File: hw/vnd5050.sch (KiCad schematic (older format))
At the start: 8 parts, among them U601 VND5050AJTR-E

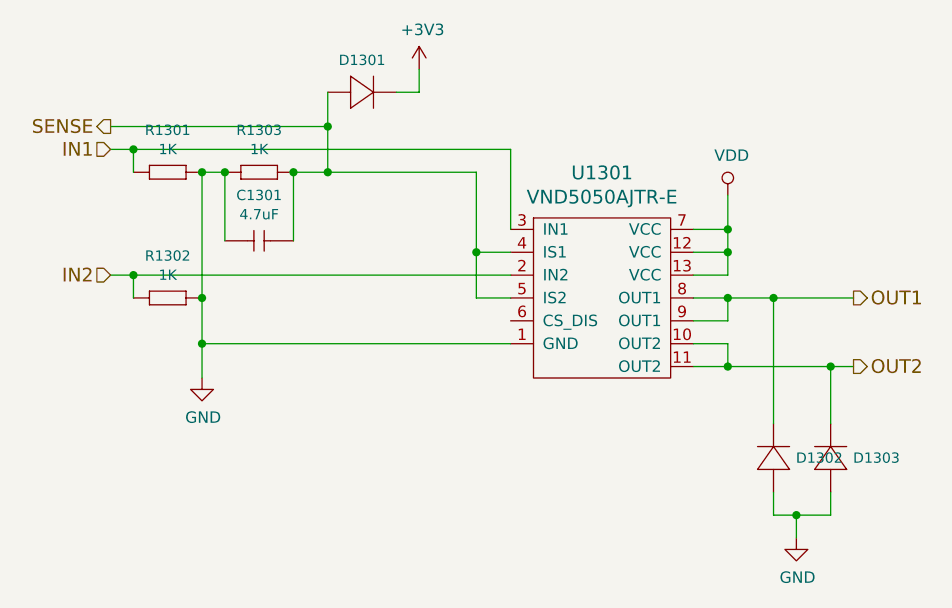
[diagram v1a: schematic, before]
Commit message: pull down resistor to boom vdd added, flyback diodes replaced with zeners
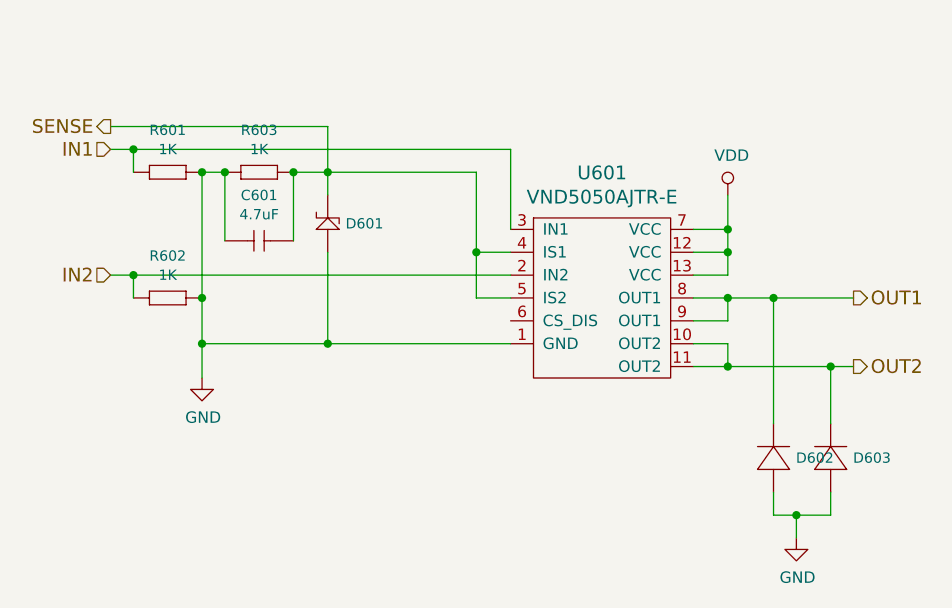
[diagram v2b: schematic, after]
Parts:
- removed D601: DIODE_RS07J-GS18, usevolt:DO219AB, symbol usevolt:DIODE_RS07J-GS18
- added D801: ZENER_MM3Z3V6T1G, usevolt:SOD-323, symbol usevolt:ZENER_MM3Z3V6T1G
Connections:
- net GND: now also D801.2
- net SENSE: now also D801.1
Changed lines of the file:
@@
 $Descr A4 11693 8268
 encoding utf-8
-Sheet 13 13
+Sheet 8 13
 Title ""
 Date ""
@@
 	2550 4000 2650 4000
 Wire Wire Line
-	2950 4300 4300 4300
+	2950 4300 3500 4300
 Wire Wire Line
 	3050 3550 2950 3550
@@
 	3350 3550 3500 3550
 Wire Wire Line
-	3500 3200 3500 3350
-Wire Wire Line
 	3500 3350 2550 3350
 Connection ~ 3500 3550
@@
 	4150 4100 4300 4100
 Connection ~ 4150 3900
-Connection ~ 3500 3350
-Wire Wire Line
-	3900 3100 3900 3200
-Wire Wire Line
-	3900 3200 3800 3200
 Wire Wire Line
 	5250 3800 5250 3900
@@
 AR Path="/5B0F1C64/5AF37914" Ref="U1201"  Part="1"
 AR Path="/5B10443F/5AF37914" Ref="U1301"  Part="1"
-F 0 "U1301" H 4700 4447 60  0000 C CNN
+F 0 "U601" H 4700 4447 60  0000 C CNN
 F 1 "VND5050AJTR-E" H 4700 4341 60  0000 C CNN
 F 2 "usevolt:PowerSSO-12" H 4600 4400 60  0001 C CNN
@@
 F 7 "VND5050AJTR-E" H 4800 4600 60  0001 C CNN "Manufacturer Part Number"
 	1    4600 4000
-	1    0    0    -1
-$EndComp
-$Comp
-L power:+3V3 #PWR0127
-U 1 1 5AF379DD
-P 3900 3100
-AR Path="/5AF2EB89/5AF379DD" Ref="#PWR0127"  Part="1"
-AR Path="/5AF65DC6/5AF379DD" Ref="#PWR0111"  Part="1"
-AR Path="/5AF66334/5AF379DD" Ref="#PWR0115"  Part="1"
-AR Path="/5AF66EB3/5AF379DD" Ref="#PWR0119"  Part="1"
-AR Path="/5AF67112/5AF379DD" Ref="#PWR0123"  Part="1"
-AR Path="/5B0F1C64/5AF379DD" Ref="#PWR01202"  Part="1"
-AR Path="/5B10443F/5AF379DD" Ref="#PWR01302"  Part="1"
-F 0 "#PWR01302" H 3900 2950 50  0001 C CNN
-F 1 "+3V3" H 3915 3273 50  0000 C CNN
-F 2 "" H 3900 3100 50  0000 C CNN
-F 3 "" H 3900 3100 50  0000 C CNN
-	1    3900 3100
-	1    0    0    -1
-$EndComp
-$Comp
-L usevolt:DIODE_RS07J-GS18 D601
-U 1 1 5AF37BFE
-P 3700 3200
-AR Path="/5AF2EB89/5AF37BFE" Ref="D601"  Part="1"
-AR Path="/5AF65DC6/5AF37BFE" Ref="D701"  Part="1"
-AR Path="/5AF66334/5AF37BFE" Ref="D801"  Part="1"
-AR Path="/5AF66EB3/5AF37BFE" Ref="D901"  Part="1"
-AR Path="/5AF67112/5AF37BFE" Ref="D1001"  Part="1"
-AR Path="/5B0F1C64/5AF37BFE" Ref="D1201"  Part="1"
-AR Path="/5B10443F/5AF37BFE" Ref="D1301"  Part="1"
-F 0 "D1301" H 3650 3340 45  0000 C CNN
-F 1 "DIODE_RS07J-GS18" H 3720 3140 45  0001 L BNN
-F 2 "usevolt:DO219AB" H 3730 3350 20  0001 C CNN
-F 3 "http://www.vishay.com/docs/85742/rs07b.pdf" H 3720 3220 60  0001 C CNN
-F 4 "1864882" H 4320 3820 60  0001 C CNN "2nd Source Part Number"
-F 5 "Digi-Key" H 4020 3520 60  0001 C CNN "1st Source"
-F 6 "Farnell" H 4220 3720 60  0001 C CNN "2nd Source"
-F 7 "RS07J-GS18" H 3920 3420 60  0001 C CNN "Manufacturer Part Number"
-F 8 "RS07J-GS18-ND" H 4120 3620 60  0001 C CNN "1st Source Part Number"
-F 9 "Vishay Semiconductor Diodes Division" H 3820 3320 60  0001 C CNN "Manufacturer"
-	1    3700 3200
 	1    0    0    -1
 $EndComp
@@
 AR Path="/5B0F1C64/5AF37D16" Ref="R1201"  Part="1"
 AR Path="/5B10443F/5AF37D16" Ref="R1301"  Part="1"
-F 0 "R1301" H 2800 3734 45  0000 C CNN
+F 0 "R601" H 2800 3734 45  0000 C CNN
 F 1 "1K" H 2800 3650 45  0000 C CNN
 F 2 "yageo:0603" H 2780 3700 20  0001 C CNN
@@
 AR Path="/5B0F1C64/5AF37DEE" Ref="R1203"  Part="1"
 AR Path="/5B10443F/5AF37DEE" Ref="R1303"  Part="1"
-F 0 "R1303" H 3200 3734 45  0000 C CNN
+F 0 "R603" H 3200 3734 45  0000 C CNN
 F 1 "1K" H 3200 3650 45  0000 C CNN
 F 2 "yageo:0603" H 3180 3700 20  0001 C CNN
@@
 AR Path="/5B0F1C64/5AF37F1E" Ref="C1201"  Part="1"
 AR Path="/5B10443F/5AF37F1E" Ref="C1301"  Part="1"
-F 0 "C1301" H 3200 4049 45  0000 C CNN
+F 0 "C601" H 3200 4049 45  0000 C CNN
 F 1 "4.7uF" H 3200 3965 45  0000 C CNN
 F 2 "kemet:0603" H 3180 4000 20  0001 C CNN
@@
 AR Path="/5B0F1C64/5AF38005" Ref="R1202"  Part="1"
 AR Path="/5B10443F/5AF38005" Ref="R1302"  Part="1"
-F 0 "R1302" H 2800 4284 45  0000 C CNN
+F 0 "R602" H 2800 4284 45  0000 C CNN
 F 1 "1K" H 2800 4200 45  0000 C CNN
 F 2 "yageo:0603" H 2780 4250 20  0001 C CNN
@@
 AR Path="/5B0F1C64/5AF380A6" Ref="#PWR01201"  Part="1"
 AR Path="/5B10443F/5AF380A6" Ref="#PWR01301"  Part="1"
-F 0 "#PWR01301" H 2950 4200 50  0001 C CNN
+F 0 "#PWR0128" H 2950 4200 50  0001 C CNN
 F 1 "GND" H 2955 4277 50  0000 C CNN
 F 2 "" H 2950 4450 50  0000 C CNN
@@
 AR Path="/5B0F1C64/5AF38434" Ref="D1202"  Part="1"
 AR Path="/5B10443F/5AF38434" Ref="D1302"  Part="1"
-F 0 "D1302" V 5400 4652 45  0000 R CNN
+F 0 "D602" V 5400 4652 45  0000 R CNN
 F 1 "DIODE_RS07J-GS18" H 5470 4690 45  0001 L BNN
 F 2 "usevolt:DO219AB" H 5480 4900 20  0001 C CNN
@@
 AR Path="/5B0F1C64/5AF384B4" Ref="D1203"  Part="1"
 AR Path="/5B10443F/5AF384B4" Ref="D1303"  Part="1"
-F 0 "D1303" V 5650 4652 45  0000 R CNN
+F 0 "D603" V 5650 4652 45  0000 R CNN
 F 1 "DIODE_RS07J-GS18" H 5720 4690 45  0001 L BNN
 F 2 "usevolt:DO219AB" H 5730 4900 20  0001 C CNN
@@
 AR Path="/5B0F1C64/5AF38539" Ref="#PWR01204"  Part="1"
 AR Path="/5B10443F/5AF38539" Ref="#PWR01304"  Part="1"
-F 0 "#PWR01304" H 5550 4900 50  0001 C CNN
+F 0 "#PWR0129" H 5550 4900 50  0001 C CNN
 F 1 "GND" H 5555 4977 50  0000 C CNN
 F 2 "" H 5550 5150 50  0000 C CNN
@@
 AR Path="/5B0F1C64/5AF38D40" Ref="#PWR01203"  Part="1"
 AR Path="/5B10443F/5AF38D40" Ref="#PWR01303"  Part="1"
-F 0 "#PWR01303" H 5250 3500 50  0001 C CNN
+F 0 "#PWR0110" H 5250 3500 50  0001 C CNN
 F 1 "VDD" H 5267 3823 50  0000 C CNN
 F 2 "" H 5250 3650 50  0000 C CNN
@@
 	1    0    0    -1
 $EndComp
+$Comp
+L usevolt:ZENER_MM3Z3V6T1G D801
+U 1 1 5B71E1C6
+P 3500 3700
+AR Path="/5AF66334/5B71E1C6" Ref="D801"  Part="1"
+AR Path="/5AF2EB89/5B71E1C6" Ref="D601"  Part="1"
+AR Path="/5AF65DC6/5B71E1C6" Ref="D701"  Part="1"
+AR Path="/5AF66EB3/5B71E1C6" Ref="D901"  Part="1"
+AR Path="/5AF67112/5B71E1C6" Ref="D1001"  Part="1"
+AR Path="/5B0F1C64/5B71E1C6" Ref="D1201"  Part="1"
+AR Path="/5B10443F/5B71E1C6" Ref="D1301"  Part="1"
+F 0 "D601" V 3425 3622 45  0000 R CNN
+F 1 "ZENER_MM3Z3V6T1G" H 3775 4075 45  0001 L BNN
+F 2 "usevolt:SOD-323" H 3475 4075 20  0001 C CNN
+F 3 "http://www.mouser.com/ds/2/308/MM3Z2V4T1-D-269162.pdf" H 3850 4275 60  0001 C CNN
+F 4 "Mouser" H 3820 4020 60  0001 C CNN "1st Source"
+F 5 "MM3Z3V6T1G" H 3720 3920 60  0001 C CNN "Manufacturer Part Number"
+F 6 "863-MM3Z3V6T1G" H 3920 4120 60  0001 C CNN "1st Source Part Number"
+F 7 "ON Semiconductor" H 3775 4175 60  0001 C CNN "Manufacturer"
+	1    3500 3700
+	0    -1   -1   0
+$EndComp
+Wire Wire Line
+	3500 3650 3500 3550
+Wire Wire Line
+	3500 3900 3500 4300
+Connection ~ 3500 4300
+Wire Wire Line
+	3500 4300 4300 4300
 $EndSCHEMATC

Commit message: tantalum cap added to mcp2515
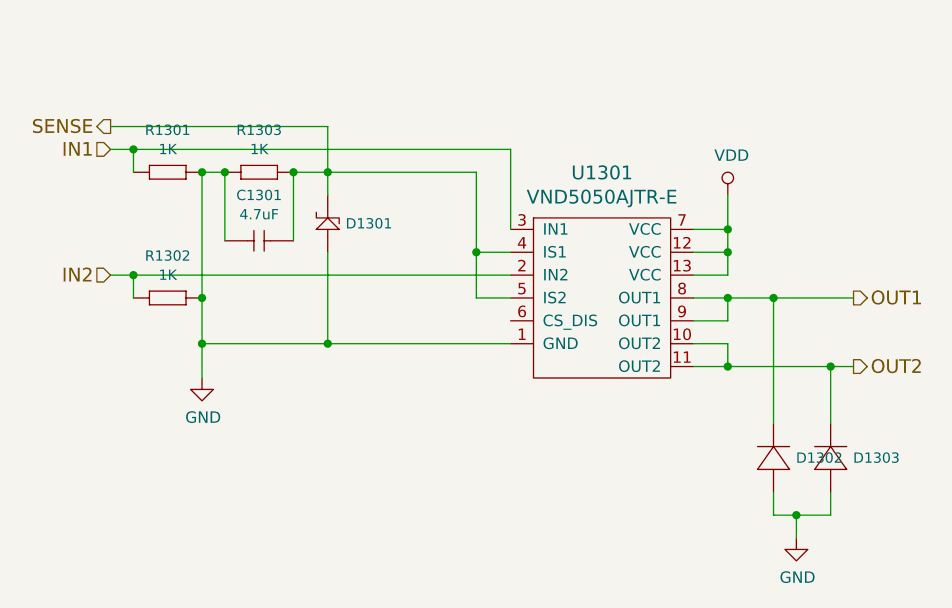
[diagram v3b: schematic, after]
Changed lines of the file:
@@
 AR Path="/5B0F1C64/5AF37914" Ref="U1201"  Part="1"
 AR Path="/5B10443F/5AF37914" Ref="U1301"  Part="1"
-F 0 "U601" H 4700 4447 60  0000 C CNN
+F 0 "U1301" H 4700 4447 60  0000 C CNN
 F 1 "VND5050AJTR-E" H 4700 4341 60  0000 C CNN
 F 2 "usevolt:PowerSSO-12" H 4600 4400 60  0001 C CNN
@@
 AR Path="/5B0F1C64/5AF37D16" Ref="R1201"  Part="1"
 AR Path="/5B10443F/5AF37D16" Ref="R1301"  Part="1"
-F 0 "R601" H 2800 3734 45  0000 C CNN
+F 0 "R1301" H 2800 3734 45  0000 C CNN
 F 1 "1K" H 2800 3650 45  0000 C CNN
 F 2 "yageo:0603" H 2780 3700 20  0001 C CNN
@@
 AR Path="/5B0F1C64/5AF37DEE" Ref="R1203"  Part="1"
 AR Path="/5B10443F/5AF37DEE" Ref="R1303"  Part="1"
-F 0 "R603" H 3200 3734 45  0000 C CNN
+F 0 "R1303" H 3200 3734 45  0000 C CNN
 F 1 "1K" H 3200 3650 45  0000 C CNN
 F 2 "yageo:0603" H 3180 3700 20  0001 C CNN
@@
 AR Path="/5B0F1C64/5AF37F1E" Ref="C1201"  Part="1"
 AR Path="/5B10443F/5AF37F1E" Ref="C1301"  Part="1"
-F 0 "C601" H 3200 4049 45  0000 C CNN
+F 0 "C1301" H 3200 4049 45  0000 C CNN
 F 1 "4.7uF" H 3200 3965 45  0000 C CNN
 F 2 "kemet:0603" H 3180 4000 20  0001 C CNN
@@
 AR Path="/5B0F1C64/5AF38005" Ref="R1202"  Part="1"
 AR Path="/5B10443F/5AF38005" Ref="R1302"  Part="1"
-F 0 "R602" H 2800 4284 45  0000 C CNN
+F 0 "R1302" H 2800 4284 45  0000 C CNN
 F 1 "1K" H 2800 4200 45  0000 C CNN
 F 2 "yageo:0603" H 2780 4250 20  0001 C CNN
@@
 AR Path="/5B0F1C64/5AF380A6" Ref="#PWR01201"  Part="1"
 AR Path="/5B10443F/5AF380A6" Ref="#PWR01301"  Part="1"
-F 0 "#PWR0128" H 2950 4200 50  0001 C CNN
+F 0 "#PWR01301" H 2950 4200 50  0001 C CNN
 F 1 "GND" H 2955 4277 50  0000 C CNN
 F 2 "" H 2950 4450 50  0000 C CNN
@@
 AR Path="/5B0F1C64/5AF38434" Ref="D1202"  Part="1"
 AR Path="/5B10443F/5AF38434" Ref="D1302"  Part="1"
-F 0 "D602" V 5400 4652 45  0000 R CNN
+F 0 "D1302" V 5400 4652 45  0000 R CNN
 F 1 "DIODE_RS07J-GS18" H 5470 4690 45  0001 L BNN
 F 2 "usevolt:DO219AB" H 5480 4900 20  0001 C CNN
@@
 AR Path="/5B0F1C64/5AF384B4" Ref="D1203"  Part="1"
 AR Path="/5B10443F/5AF384B4" Ref="D1303"  Part="1"
-F 0 "D603" V 5650 4652 45  0000 R CNN
+F 0 "D1303" V 5650 4652 45  0000 R CNN
 F 1 "DIODE_RS07J-GS18" H 5720 4690 45  0001 L BNN
 F 2 "usevolt:DO219AB" H 5730 4900 20  0001 C CNN
@@
 AR Path="/5B0F1C64/5AF38539" Ref="#PWR01204"  Part="1"
 AR Path="/5B10443F/5AF38539" Ref="#PWR01304"  Part="1"
-F 0 "#PWR0129" H 5550 4900 50  0001 C CNN
+F 0 "#PWR01304" H 5550 4900 50  0001 C CNN
 F 1 "GND" H 5555 4977 50  0000 C CNN
 F 2 "" H 5550 5150 50  0000 C CNN
@@
 AR Path="/5B0F1C64/5AF38D40" Ref="#PWR01203"  Part="1"
 AR Path="/5B10443F/5AF38D40" Ref="#PWR01303"  Part="1"
-F 0 "#PWR0110" H 5250 3500 50  0001 C CNN
+F 0 "#PWR01303" H 5250 3500 50  0001 C CNN
 F 1 "VDD" H 5267 3823 50  0000 C CNN
 F 2 "" H 5250 3650 50  0000 C CNN
@@
 AR Path="/5B0F1C64/5B71E1C6" Ref="D1201"  Part="1"
 AR Path="/5B10443F/5B71E1C6" Ref="D1301"  Part="1"
-F 0 "D601" V 3425 3622 45  0000 R CNN
+F 0 "D1301" V 3425 3622 45  0000 R CNN
 F 1 "ZENER_MM3Z3V6T1G" H 3775 4075 45  0001 L BNN
 F 2 "usevolt:SOD-323" H 3475 4075 20  0001 C CNN
